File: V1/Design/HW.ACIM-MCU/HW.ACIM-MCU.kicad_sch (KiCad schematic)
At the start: 41 parts, among them J1 HEADER 2x15POS, J2 HEADER 2x15POS, U1 MIPS 32-bit DSC, U2 12MHz (3225), X1 32.768kHz

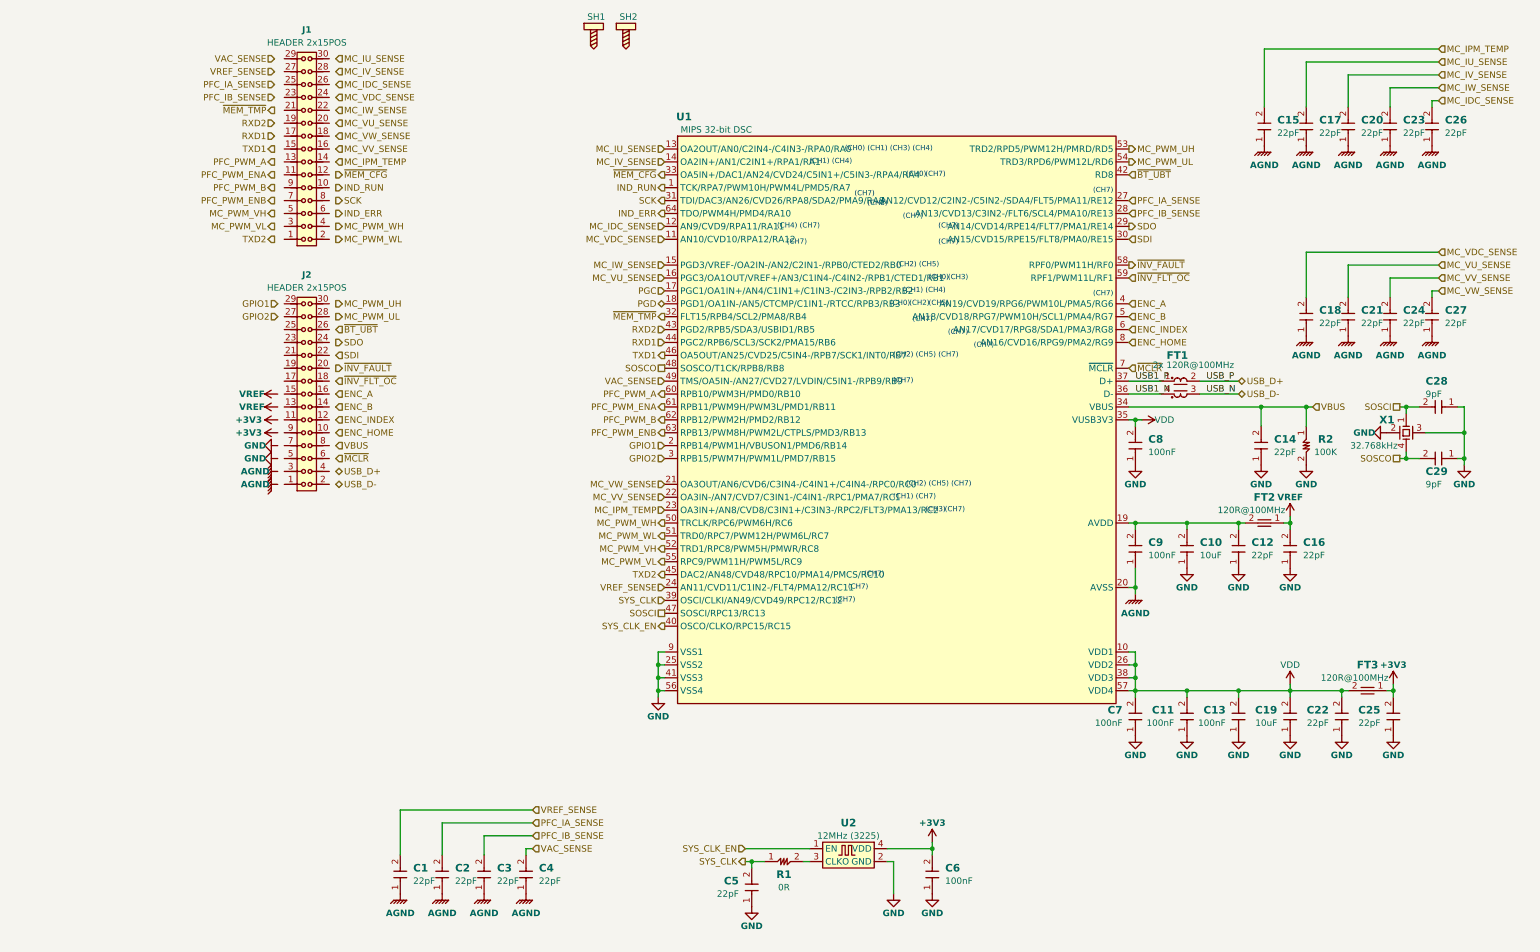
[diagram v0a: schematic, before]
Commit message: MCU PIM schematic update 1
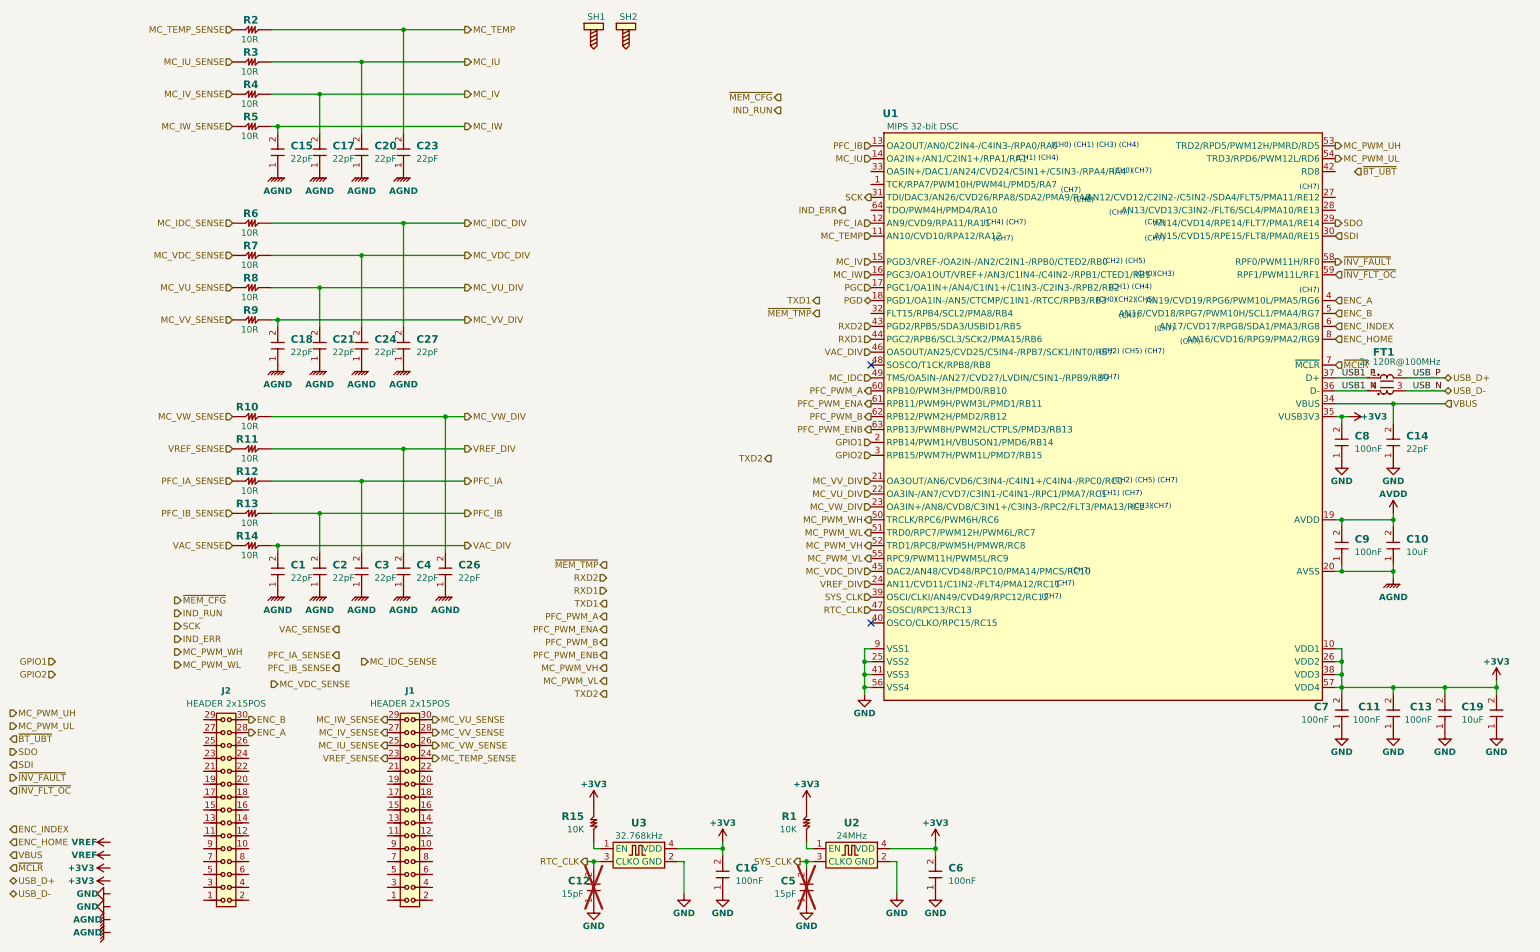
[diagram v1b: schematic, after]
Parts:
- removed C22, C25: 22pF, SAMPI:CAP0603, symbol SAMPI:CERCAP
- removed C28, C29: 9pF, SAMPI:CAP0603, symbol SAMPI:CERCAP
- removed FT2, FT3: 120R@100MHz, SAMPI:FT0603, symbol SAMPI:FerriteBead
- removed X1: 32.768kHz, SAMPI:SMD4-7015, symbol SAMPI:XTAL-4P
- added R10, R11, R12, R13, R14, R3, R4, R5, R6, R7, R8, R9: 10R, symbol SAMPI:RES
- added R15: 10K, symbol SAMPI:RES
- added U3: 32.768kHz, SAMPI:CDFN3225-4LD-PL-1, symbol SAMPI:OSC
- C12, C5: value 22pF -> 15pF; now not fitted; now left out of the parts list
- C16: value 22pF -> 100nF; MFT Walsin -> Samsung; MNP 0603N220J500CT -> CL10B104KB8NNNC; Unit Price 0.012 -> 0.0146
- R1: value 0R -> 10K; footprint SAMPI:RES0603 -> (none); Checked OK -> (none); MFT YAGEO -> (none); MNP RC0603JR-070RL -> (none); Unit Price 0.015 -> (none)
- R2: value 100K -> 10R; footprint SAMPI:RES0603 -> (none); Checked OK -> (none); MFT YAGEO -> (none); MNP RC0603FR-07100KL -> (none); Unit Price 0.019 -> (none)
- U2: value 12MHz (3225) -> 24MHz; MFT Microchip -> Abracon LLC; MNP DSC1001CE1-012.0000 -> ASEDV-24.000MHZ-LR-T; Unit Price 1.15 -> 1.06
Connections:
- net VDD is gone; now on net +3V3: C11.2, C13.2, C19.2, C7.2, C8.2, U1.10 (VDD1), U1.26 (VDD2), U1.35 (VUSB3V3), U1.38 (VDD3), U1.57 (VDD4)
- net +3V3: now also C16.2, R1.2, R15.2, U3.4 (VDD)
- net AGND: now also C10.1
- net ENC_A: now also J2.28
- net ENC_B: now also J2.30
- net GND: now also U3.2 (GND); no longer C10.1, R2.2
- net IND_ERR: no longer U1.64 (TDO/PWM4H/PMD4/RA10)
- net IND_RUN: no longer U1.1 (TCK/RPA7/PWM10H/PWM4L/PMD5/RA7)
- net MC_IDC_SENSE: now also R6.1; no longer C26.2, U1.12 (AN9/CVD9/RPA11/RA11)
- net MC_IU_SENSE: now also J1.25, R3.1; no longer C17.2, U1.13 (OA2OUT/AN0/C2IN4-/C4IN3-/RPA0/RA0)
- net MC_IV_SENSE: now also J1.27, R4.1; no longer C20.2, U1.14 (OA2IN+/AN1/C2IN1+/RPA1/RA1)
- net MC_IW_SENSE: now also J1.29, R5.1; no longer C23.2, U1.15 (PGD3/VREF-/OA2IN-/AN2/C2IN1-/RPB0/CTED2/RB0)
- net MC_VDC_SENSE: now also R7.1; no longer C18.2, U1.11 (AN10/CVD10/RPA12/RA12)
- net MC_VU_SENSE: now also J1.30, R8.1; no longer C21.2, U1.16 (PGC3/OA1OUT/VREF+/AN3/C1IN4-/C4IN2-/RPB1/CTED1/RB1)
- net MC_VV_SENSE: now also J1.28, R9.1; no longer C24.2, U1.22 (OA3IN-/AN7/CVD7/C3IN1-/C4IN1-/RPC1/PMA7/RC1)
- net MC_VW_SENSE: now also J1.26, R10.1; no longer C27.2, U1.21 (OA3OUT/AN6/CVD6/C3IN4-/C4IN1+/C4IN4-/RPC0/RC0)
- net PFC_IA_SENSE: now also R12.1; no longer C2.2, U1.27 (AN12/CVD12/C2IN2-/C5IN2-/SDA4/FLT5/PMA11/RE12)
- net PFC_IB_SENSE: now also R13.1; no longer C3.2, U1.28 (AN13/CVD13/C3IN2-/FLT6/SCL4/PMA10/RE13)
- net SYS_CLK: now also U2.3 (CLKO); no longer R1.1
- net TXD1: no longer U1.46 (OA5OUT/AN25/CVD25/C5IN4-/RPB7/SCK1/INT0/RB7)
- net TXD2: no longer U1.45 (DAC2/AN48/CVD48/RPC10/PMA14/PMCS/RC10)
- net VAC_SENSE: now also R14.1; no longer C4.2, U1.49 (TMS/OA5IN-/AN27/CVD27/LVDIN/C5IN1-/RPB9/RB9)
- net VBUS: no longer R2.1
- net VREF: no longer C16.2
- net VREF_SENSE: now also J1.23, R11.1; no longer C1.2, U1.24 (AN11/CVD11/C1IN2-/FLT4/PMA12/RC11)
- net ~{BT_UBT}: no longer U1.42 (RD8)
- net ~{MEM_CFG}: no longer U1.33 (OA5IN+/DAC1/AN24/CVD24/C5IN1+/C5IN3-/RPA4/RA4)
- net ~{MEM_TMP}: no longer U1.32 (FLT15/RPB4/SCL2/PMA8/RB4)
- net AVDD: now reaches C10.2, C9.2, U1.19 (AVDD)
- net AVDD: no longer C12.2
- net MC_TEMP_SENSE: now reaches J1.24
- net MC_TEMP_SENSE: now also R2.1
- net MC_IPM_TEMP renamed MC_IW
- net MC_IW: now also U1.16 (PGC3/OA1OUT/VREF+/AN3/C1IN4-/C4IN2-/RPB1/CTED1/RB1), R5.2; no longer U1.23 (OA3IN+/AN8/CVD8/C3IN1+/C3IN3-/RPC2/FLT3/PMA13/RC2)
- net SOSCI renamed RTC_CLK
- net RTC_CLK: now also C12.2, U3.3 (CLKO)
- net SOSCO: no longer names the net of U1.48 (SOSCO/T1CK/RPB8/RB8)
- net SYS_CLK_EN: no longer names the net of U2.1 (EN)
- net SYS_CLK_EN: now also R1.1; no longer U1.40 (OSCO/CLKO/RPC15/RC15)
- new net: R15.1, U3.1 (EN)
- new net MC_IDC: U1.49 (TMS/OA5IN-/AN27/CVD27/LVDIN/C5IN1-/RPB9/RB9)
- new net MC_IDC_DIV: C27.2, R6.2
- new net MC_IU: C20.2, R3.2, U1.14 (OA2IN+/AN1/C2IN1+/RPA1/RA1)
- new net MC_IV: C17.2, R4.2, U1.15 (PGD3/VREF-/OA2IN-/AN2/C2IN1-/RPB0/CTED2/RB0)
- new net MC_TEMP: C23.2, R2.2, U1.11 (AN10/CVD10/RPA12/RA12)
- new net MC_VDC_DIV: C24.2, R7.2, U1.45 (DAC2/AN48/CVD48/RPC10/PMA14/PMCS/RC10)
- new net MC_VU_DIV: C21.2, R8.2, U1.22 (OA3IN-/AN7/CVD7/C3IN1-/C4IN1-/RPC1/PMA7/RC1)
- new net MC_VV_DIV: C18.2, R9.2, U1.21 (OA3OUT/AN6/CVD6/C3IN4-/C4IN1+/C4IN4-/RPC0/RC0)
- new net MC_VW_DIV: C26.2, R10.2, U1.23 (OA3IN+/AN8/CVD8/C3IN1+/C3IN3-/RPC2/FLT3/PMA13/RC2)
- new net PFC_IA: C3.2, R12.2, U1.12 (AN9/CVD9/RPA11/RA11)
- new net PFC_IB: C2.2, R13.2, U1.13 (OA2OUT/AN0/C2IN4-/C4IN3-/RPA0/RA0)
- new net VAC_DIV: C1.2, R14.2, U1.46 (OA5OUT/AN25/CVD25/C5IN4-/RPB7/SCK1/INT0/RB7)
- new net VREF_DIV: C4.2, R11.2, U1.24 (AN11/CVD11/C1IN2-/FLT4/PMA12/RC11)
- no-connect marks 0 -> 2
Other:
- moved on the sheet: C1, C10, C11, C13, C14, C15, C17, C18, C19, C2, C20, C21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

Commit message: MCU PIM schematic update 3
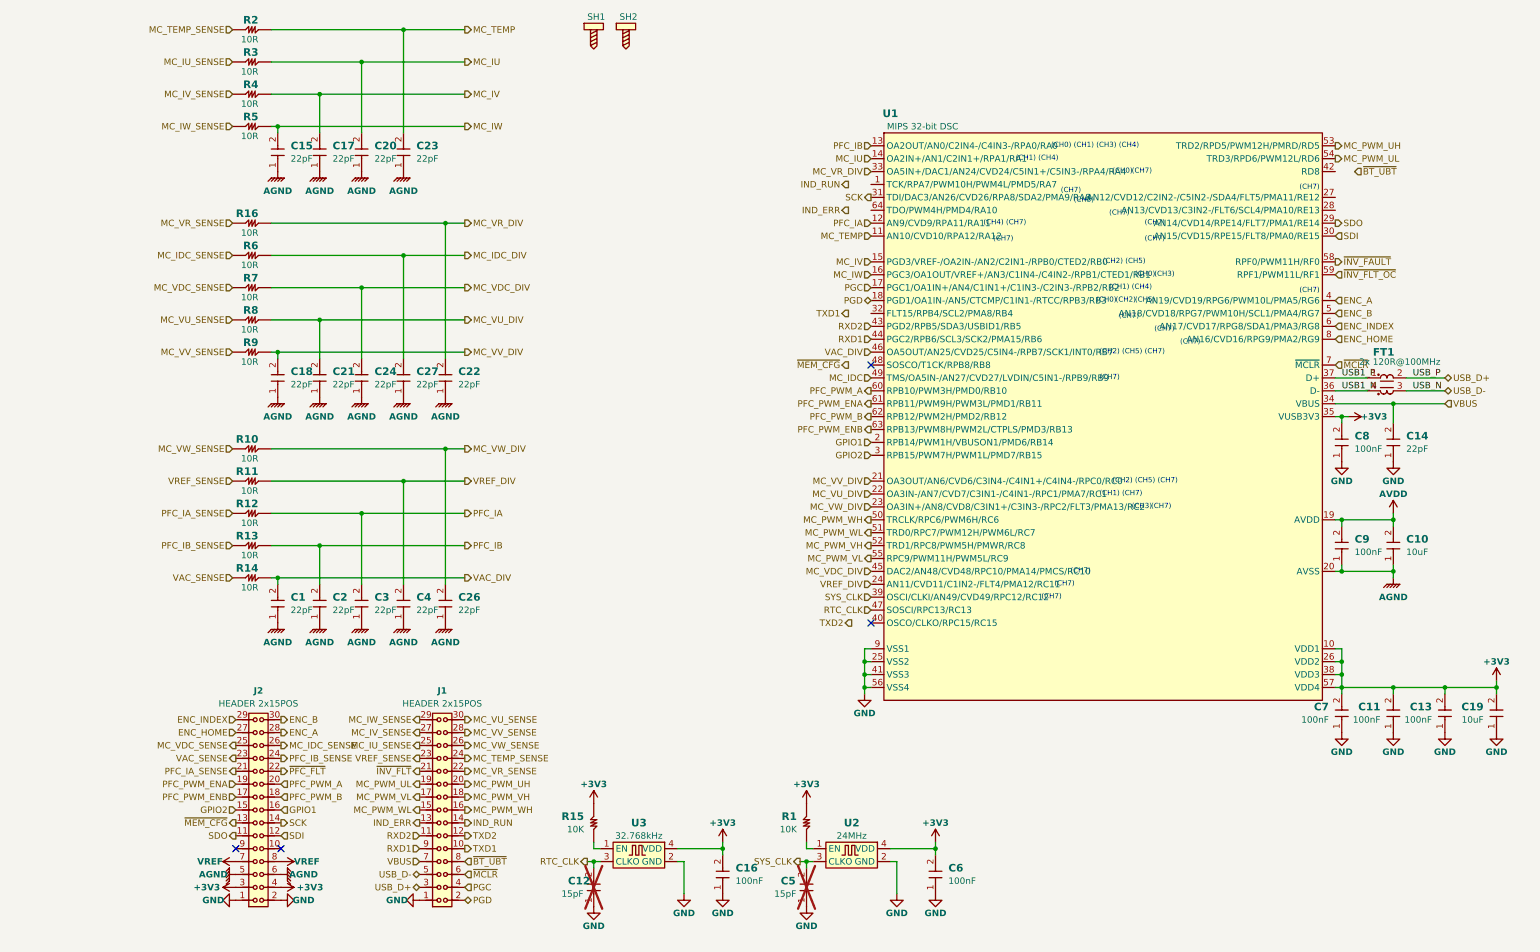
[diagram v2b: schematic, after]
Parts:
- added C22: 22pF, SAMPI:CAP0402, symbol SAMPI:CERCAP
- added R16: 10R, SAMPI:RES0402, symbol SAMPI:RES
- C1, C14, C15, C17, C18, C2, C20, C21, C23, C24, C26, C27, C3, C4: footprint SAMPI:CAP0603 -> SAMPI:CAP0402; Checked OK -> (none); Unit Price 0.012 -> (none)
- C10, C19: Checked OK -> (none); Unit Price 0.079 -> (none)
- C11, C13, C16, C6, C7, C8, C9: footprint SAMPI:CAP0603 -> SAMPI:CAP0402; Checked OK -> (none); Unit Price 0.0146 -> (none)
- C12, C5: Checked OK -> (none); Unit Price 0.012 -> (none)
- FT1: Checked OK -> (none); Unit Price 0.087 -> (none)
- R1, R10, R11, R12, R13, R14, R15, R2, R3, R4, R5, R6, R7, R8, R9: footprint (none) -> SAMPI:RES0402
- SH1, SH2: footprint Liem:HOLDER-3MM -> Liem:HOLDER-2.2MM
- U1: Checked OK -> (none); Unit Price 10.07 -> (none)
- U2: Checked OK -> (none); Unit Price 1.06 -> (none)
- U3: Checked OK -> (none); Unit Price 1.08 -> (none)
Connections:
- net +3V3: now also J2.3, J2.4
- net AGND: now also J2.5, J2.6, C22.1
- net ENC_HOME: now also J2.27
- net ENC_INDEX: now also J2.29
- net GND: now also J1.1, J2.1, J2.2
- net GPIO1: now also J2.16
- net GPIO2: now also J2.15
- net IND_ERR: now also J1.13
- net IND_RUN: now also J1.14
- net MC_IDC_SENSE: now also J2.26
- net MC_PWM_UH: now also J1.20
- net MC_PWM_UL: now also J1.19
- net MC_PWM_VH: now also J1.18
- net MC_PWM_VL: now also J1.17
- net MC_PWM_WH: now also J1.16
- net MC_PWM_WL: now also J1.15
- net MC_VDC_SENSE: now also J2.25
- net PFC_IA_SENSE: now also J2.21
- net PFC_IB_SENSE: now also J2.24
- net PFC_PWM_A: now also J2.20
- net PFC_PWM_B: now also J2.18
- net PFC_PWM_ENA: now also J2.19
- net PFC_PWM_ENB: now also J2.17
- net PGC: now also J1.4
- net PGD: now also J1.2
- net RXD1: now also J1.9
- net RXD2: now also J1.11
- net SCK: now also J2.14
- net SDI: now also J2.12
- net SDO: now also J2.11
- net TXD1: now also J1.10
- net TXD2: now also J1.12
- net USB_D+: now also J1.3
- net USB_D-: now also J1.5
- net VAC_SENSE: now also J2.23
- net VBUS: now also J1.7
- net VREF: now also J2.7, J2.8
- net ~{BT_UBT}: now also J1.8
- net ~{MCLR}: now also J1.6
- net ~{MEM_CFG}: now also J2.13
- net ~{INV_FLT}: now reaches J1.21
- net MC_VR_SENSE: now reaches J1.22
- net MC_VR_SENSE: now also R16.1
- net ~{PFC_FLT}: now reaches J2.22
- net MC_VR_DIV: now reaches U1.33 (OA5IN+/DAC1/AN24/CVD24/C5IN1+/C5IN3-/RPA4/RA4)
- net MC_VR_DIV: now also C22.2, R16.2
- no-connect marks 2 -> 4
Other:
- moved on the sheet: C1, C18, C2, C21, C24, C26, C27, C3, C4, J1, J2, R10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

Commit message: MCU PIM schematic update 4
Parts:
- removed C11, C16, C6: 100nF, SAMPI:CAP0402, symbol SAMPI:CERCAP
- removed C12, C5: 15pF, SAMPI:CAP0603, symbol SAMPI:CERCAP
- removed FT1: 2x 120R@100MHz, SAMPI:IND1210_4P, symbol SAMPI:IND1210_4P
- removed R1, R15: 10K, SAMPI:RES0402, symbol SAMPI:RES
- removed U2: 24MHz, SAMPI:CDFN3225-4LD-PL-1, symbol SAMPI:OSC
- removed U3: 32.768kHz, SAMPI:CDFN3225-4LD-PL-1, symbol SAMPI:OSC
- added C19, C20: 22pF, SAMPI:CAP0402, symbol SAMPI:CERCAP
- added C22, C26, C28: 10uF, SAMPI:CAP0402, symbol SAMPI:CERCAP
- added C25, C27: 100nF, SAMPI:CAP0402, symbol SAMPI:CERCAP
- added U2: 12MHz, SAMPI:SMD4-2520, symbol SAMPI:XTAL-4P
- C1: renamed from C15; MFT Walsin -> (none); MNP 0603N220J500CT -> (none)
- C10: renamed from C8; MFT Samsung -> Murata; MNP CL10B104KB8NNNC -> GRM155R71H104ME14D
- C11: renamed from C14; MFT Walsin -> (none); MNP 0603N220J500CT -> (none)
- C12: renamed from C9; MFT Samsung -> Murata; MNP CL10B104KB8NNNC -> GRM155R71H104ME14D
- C13: renamed from C10; footprint SAMPI:CAP0603 -> SAMPI:CAP0402; MFT Samsung -> Murata; MNP CL10A106MQ8NNNC -> GRM155C80J106ME11D
- C14: renamed from C1; MFT Walsin -> (none); MNP 0603N220J500CT -> (none)
- C15: renamed from C2; MFT Walsin -> (none); MNP 0603N220J500CT -> (none)
- C16: renamed from C3; MFT Walsin -> (none); MNP 0603N220J500CT -> (none)
- C17: renamed from C4; MFT Walsin -> (none); MNP 0603N220J500CT -> (none)
- C18: renamed from C26; MFT Walsin -> (none); MNP 0603N220J500CT -> (none)
- C2: renamed from C17; MFT Walsin -> (none); MNP 0603N220J500CT -> (none)
- C21: renamed from C7; MFT Samsung -> Murata; MNP CL10B104KB8NNNC -> GRM155R71H104ME14D
- C23: renamed from C13; MFT Samsung -> Murata; MNP CL10B104KB8NNNC -> GRM155R71H104ME14D
- C24: renamed from C19; footprint SAMPI:CAP0603 -> SAMPI:CAP0402; MFT Samsung -> Murata; MNP CL10A106MQ8NNNC -> GRM155C80J106ME11D
- C3: renamed from C20; MFT Walsin -> (none); MNP 0603N220J500CT -> (none)
- C4: renamed from C23; MFT Walsin -> (none); MNP 0603N220J500CT -> (none)
- C5: renamed from C18; MFT Walsin -> (none); MNP 0603N220J500CT -> (none)
- C6: renamed from C21; MFT Walsin -> (none); MNP 0603N220J500CT -> (none)
- C7: renamed from C24; MFT Walsin -> (none); MNP 0603N220J500CT -> (none)
- C8: renamed from C27; MFT Walsin -> (none); MNP 0603N220J500CT -> (none)
- C9: renamed from C22; MFT Walsin -> (none); MNP 0603N220J500CT -> (none)
- renumbered J2 to J1, J1 to J2, R2 to R1, R3 to R2, R4 to R3, R5 to R4, R16 to R5
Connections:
- net USB_D+ is gone; now on net USB_P: J2.3
- net USB_D- is gone; now on net USB_N: J2.5
- net +3V3: now also C22.2, C25.2, C26.2, C27.2, C28.2
- net GND: now also C19.1, C20.1, C22.1, C25.1, C26.1, C27.1, C28.1, U2.2 (GND1), U2.4 (GND2)
- net at U1.40 (OSCO/CLKO/RPC15/RC15): now also C20.2, U2.3 (X2)
- net RTC_CLK: no longer names the net of U1.47 (SOSCI/RPC13/RC13)
- net SYS_CLK: no longer names the net of U1.39 (OSCI/CLKI/AN49/CVD49/RPC12/RC12)
- net SYS_CLK: now also C19.2, U2.1 (X1)
- net USB1_N renamed USB_N
- net USB1_P renamed USB_P
- no-connect marks 4 -> 2
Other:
- moved on the sheet: C10, C11, C12, C13, C21, C23, C24, U1
